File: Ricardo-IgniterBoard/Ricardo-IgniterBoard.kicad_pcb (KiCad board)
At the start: 4 copper layers, 76 parts, among them J1 RBUS, J2 USB_C_Receptacle_USB2.0, U1 ESP32-S3, U2 SN65HVD230, U3 LM66200DRLR, U4 MAX77827AEFD+T, U5 SC4215ASTRT, Y1 R940000171

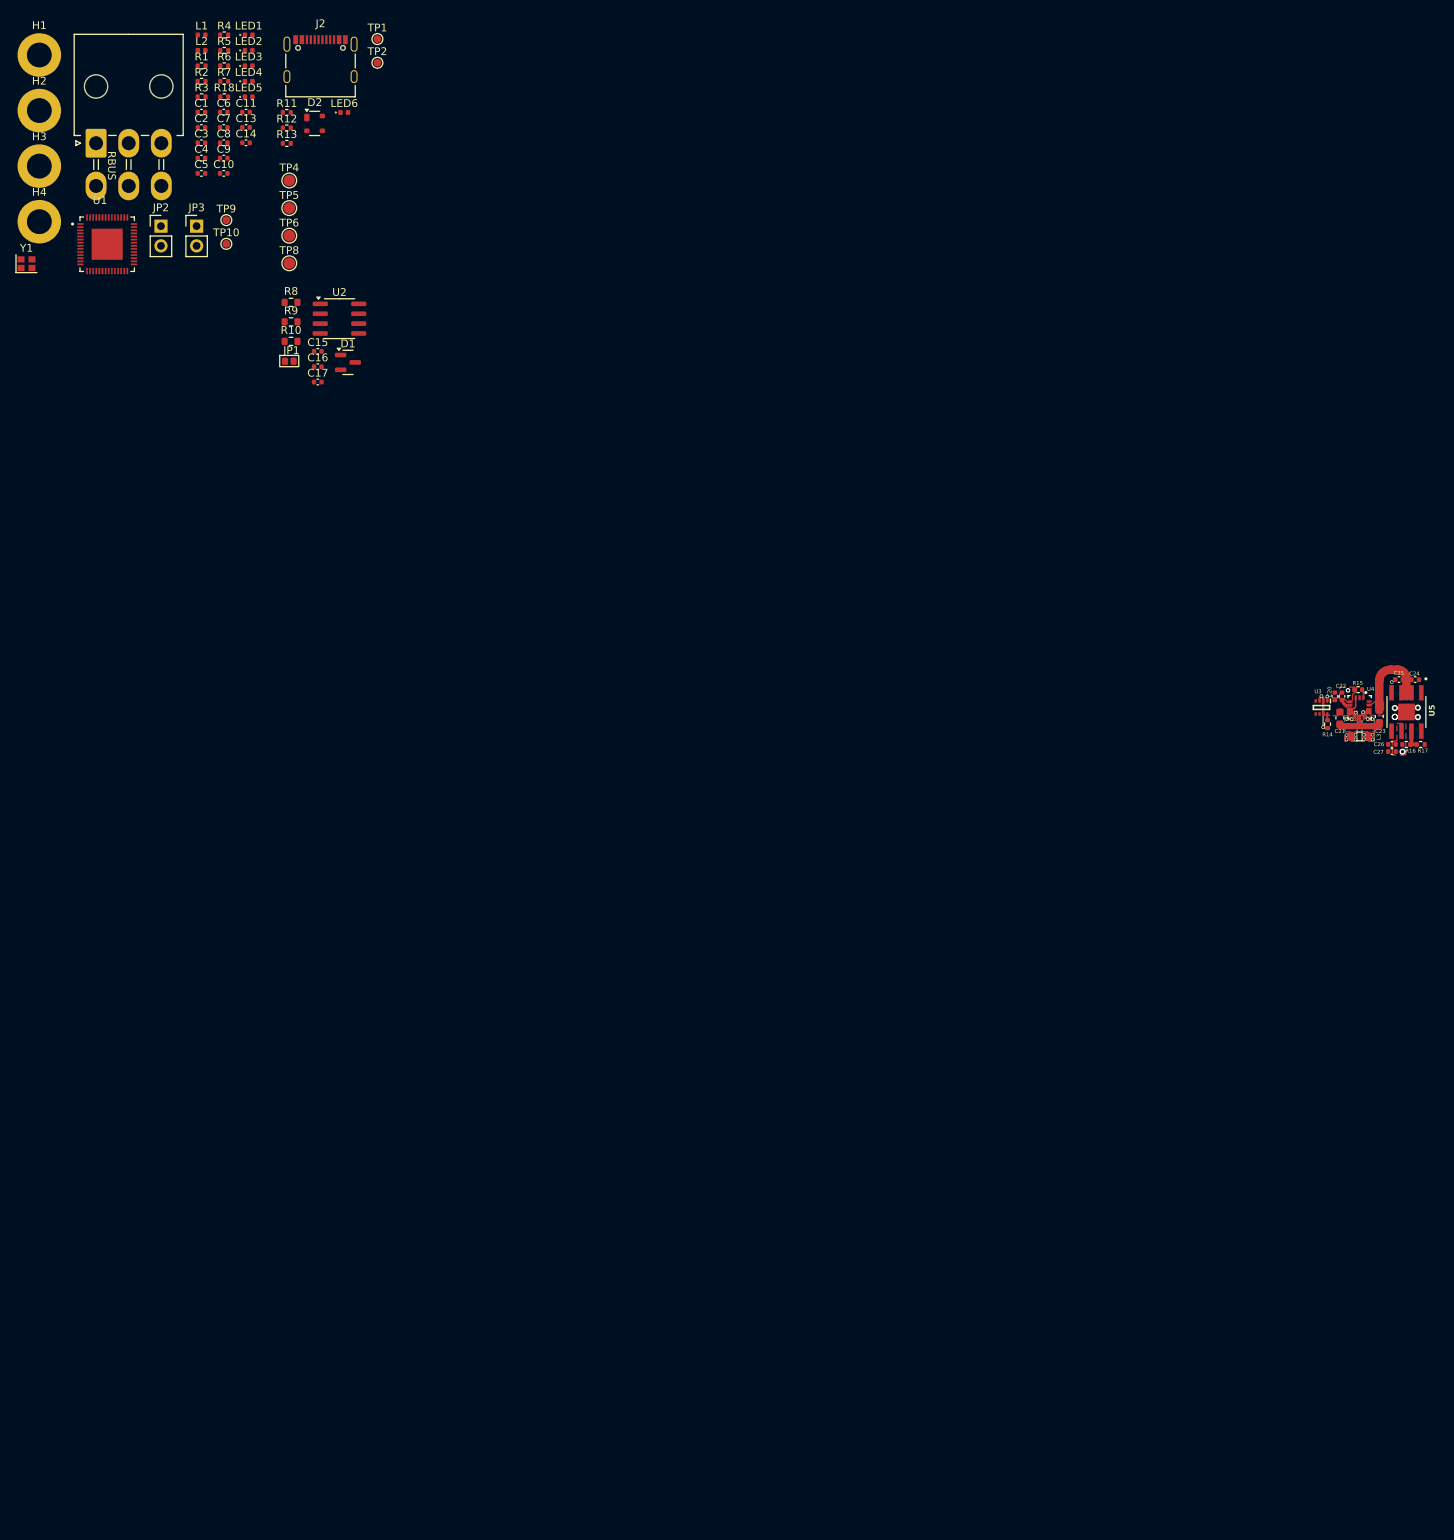
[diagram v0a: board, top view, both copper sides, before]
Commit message: Assigning components
And added the thermocouple
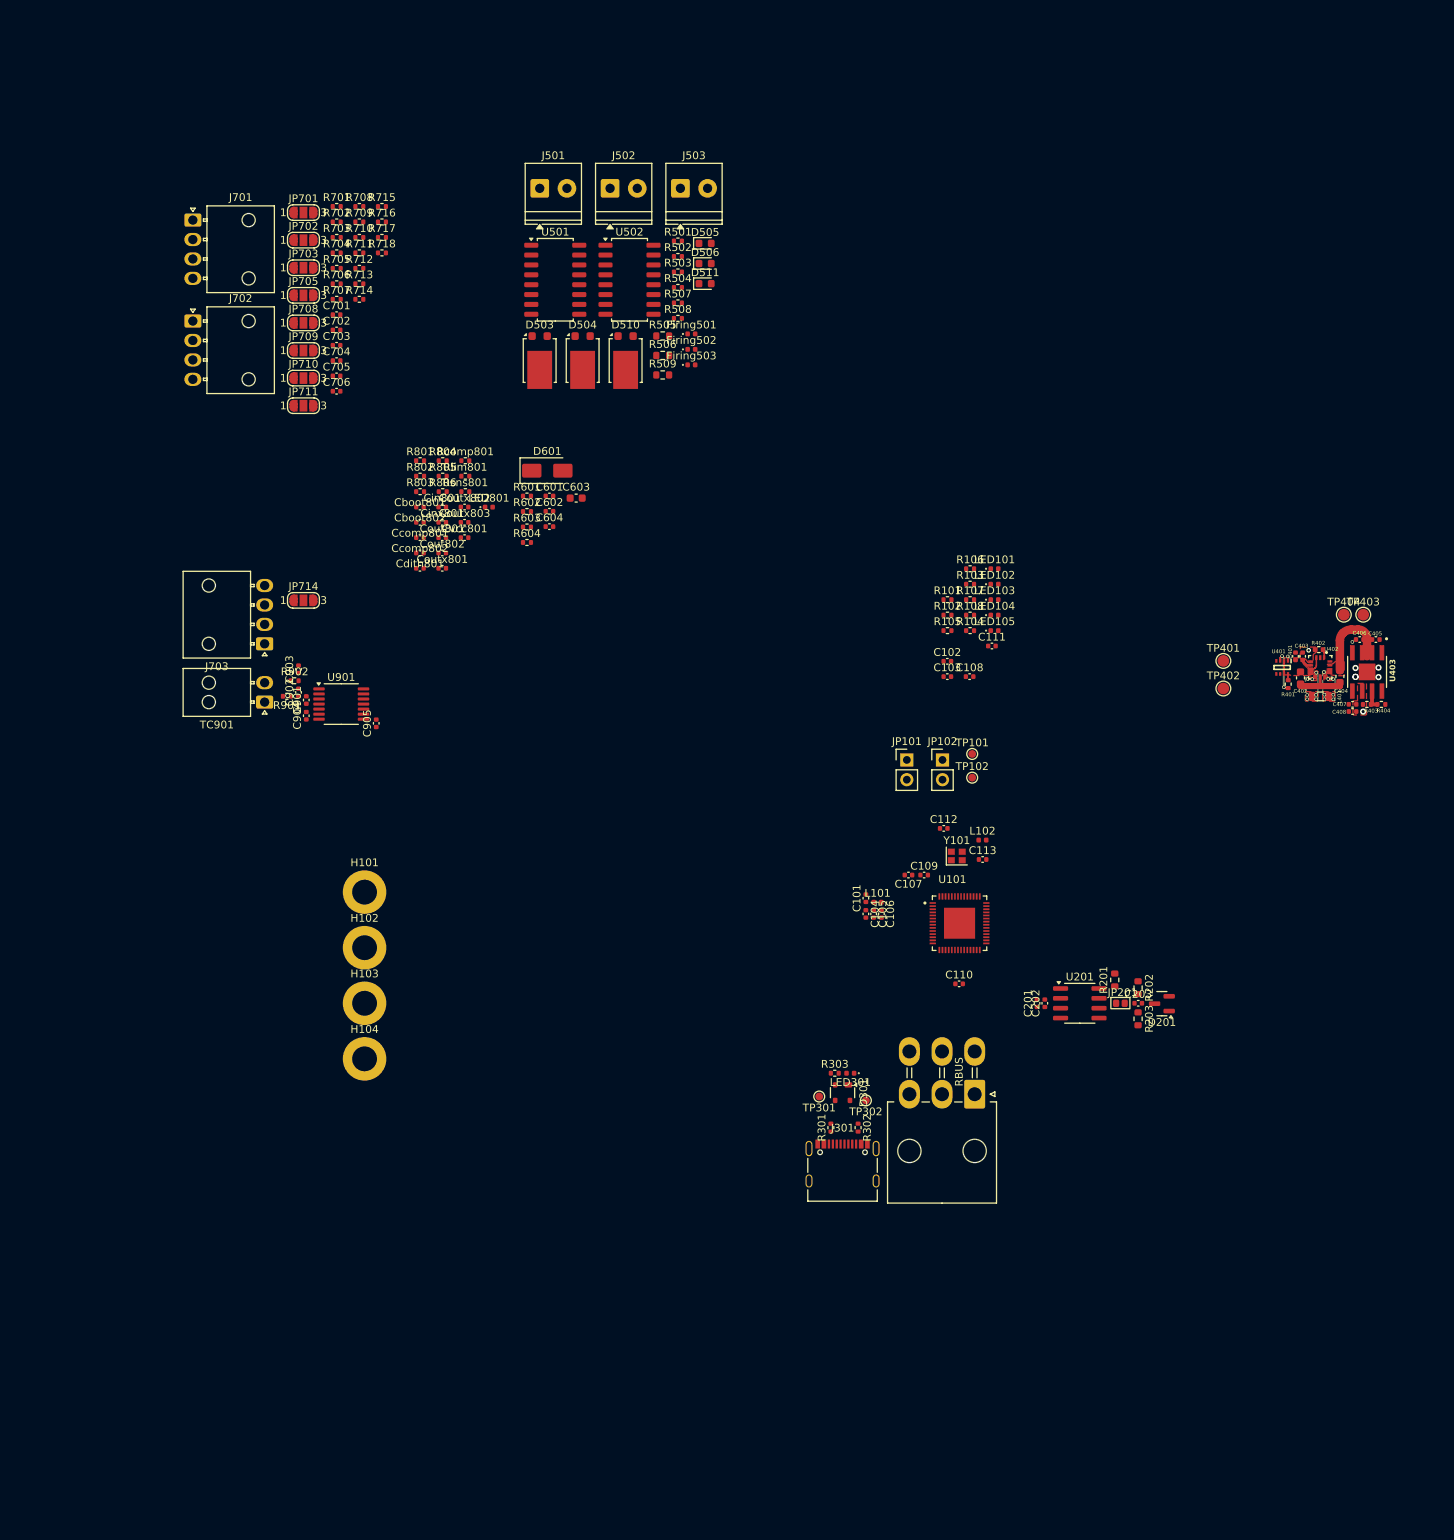
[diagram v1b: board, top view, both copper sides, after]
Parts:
- added C601: 0.1uF, Capacitor_SMD:C_0402_1005Metric, F.Cu at (68.7, 59.8)
- added C602: 1uF, Capacitor_SMD:C_0402_1005Metric, F.Cu at (68.7, 61.8)
- added C603: 0.1uF, Capacitor_SMD:C_0603_1608Metric, F.Cu at (72.2, 60.1)
- added C604: 0.1uF, Capacitor_SMD:C_0402_1005Metric, F.Cu at (68.7, 63.8)
- added C701: 1uF, Capacitor_SMD:C_0402_1005Metric, F.Cu at (41.3, 36.5)
- added C702: 1uF, Capacitor_SMD:C_0402_1005Metric, F.Cu at (41.3, 38.5)
- added C703: 220nF, Capacitor_SMD:C_0402_1005Metric, F.Cu at (41.3, 40.4)
- added C704: 10nF, Capacitor_SMD:C_0402_1005Metric, F.Cu at (41.3, 42.4)
- added C705: 10nF, Capacitor_SMD:C_0402_1005Metric, F.Cu at (41.3, 44.4)
- added C706: 10nF, Capacitor_SMD:C_0402_1005Metric, F.Cu at (41.3, 46.3)
- added C901: 0.01uF, Capacitor_SMD:C_0402_1005Metric, F.Cu at (37.4, 86.1)
- added C902: 0.1uF, Capacitor_SMD:C_0402_1005Metric, F.Cu at (36.4, 85.1)
- added C903: 0.01uF, Capacitor_SMD:C_0402_1005Metric, F.Cu at (36.4, 82.1)
- added C904: 0.1uF, Capacitor_SMD:C_0402_1005Metric, F.Cu at (37.4, 88.1)
- added C905: 0.1uF, Capacitor_SMD:C_0402_1005Metric, F.Cu at (46.4, 89.1)
- added Cboot801: 100nF, Capacitor_SMD:C_0402_1005Metric, F.Cu at (52.0, 61.2)
- added Cboot802: 100nF, Capacitor_SMD:C_0402_1005Metric, F.Cu at (52.0, 63.2)
- added Ccomp801: 15pF, Capacitor_SMD:C_0402_1005Metric, F.Cu at (52.0, 65.2)
- added Ccomp802: 2.2nF, Capacitor_SMD:C_0402_1005Metric, F.Cu at (52.0, 67.2)
- added Cdith801: 8.2nF, Capacitor_SMD:C_0402_1005Metric, F.Cu at (52.0, 69.1)
- added Cin801: 82uF, Capacitor_SMD:C_0402_1005Metric, F.Cu at (54.9, 61.2)
- added Cinx801: 10uF, Capacitor_SMD:C_0402_1005Metric, F.Cu at (54.9, 63.2)
- added Cout801: 56uF, Capacitor_SMD:C_0402_1005Metric, F.Cu at (54.9, 65.2)
- added Cout802: 56uF, Capacitor_SMD:C_0402_1005Metric, F.Cu at (54.9, 67.2)
- added Coutx801: 15uF, Capacitor_SMD:C_0402_1005Metric, F.Cu at (54.9, 69.1)
- added Coutx802: 15uF, Capacitor_SMD:C_0402_1005Metric, F.Cu at (57.8, 61.2)
- added Coutx803: 15uF, Capacitor_SMD:C_0402_1005Metric, F.Cu at (57.8, 63.2)
- added Cvcc801: 4.7uF, Capacitor_SMD:C_0402_1005Metric, F.Cu at (57.8, 65.2)
- added D503: DST1550S, Package_TO_SOT_SMD:TO-277B, F.Cu at (67.5, 42.4)
- added D504: DST1550S, Package_TO_SOT_SMD:TO-277B, F.Cu at (73.0, 42.4)
- added D505: RED_LED, LED_SMD:LED_0603_1608Metric, F.Cu at (88.7, 27.3)
- added D506: RED_LED, LED_SMD:LED_0603_1608Metric, F.Cu at (88.7, 29.9)
- added D510: DST1550S, Package_TO_SOT_SMD:TO-277B, F.Cu at (78.5, 42.4)
- added D511: RED_LED, LED_SMD:LED_0603_1608Metric, F.Cu at (88.7, 32.5)
- added D601: P6SMBJ28CA, Diode_SMD:D_SMA, F.Cu at (68.4, 56.6)
- added Firing501: EMERALD_LED, LED_SMD:LED_0402_1005Metric, F.Cu at (87.0, 39.0)
- added Firing502: EMERALD_LED, LED_SMD:LED_0402_1005Metric, F.Cu at (87.0, 41.0)
- added Firing503: EMERALD_LED, LED_SMD:LED_0402_1005Metric, F.Cu at (87.0, 42.9)
- added J501: Conn_01x02_Male, TerminalBlock_Phoenix:TerminalBlock_Phoenix_PT-1,5-2-3.5-H_1x02_P3.50mm_Horizontal, F.Cu at (67.5, 20.2)
- added J502: Conn_01x02_Male, TerminalBlock_Phoenix:TerminalBlock_Phoenix_PT-1,5-2-3.5-H_1x02_P3.50mm_Horizontal, F.Cu at (76.5, 20.2)
- added J503: Conn_01x02_Male, TerminalBlock_Phoenix:TerminalBlock_Phoenix_PT-1,5-2-3.5-H_1x02_P3.50mm_Horizontal, F.Cu at (85.6, 20.2)
- added J701: 1053131104, Connector_Molex:Molex_Nano-Fit_105313-xx04_1x04_P2.50mm_Horizontal, F.Cu at (22.8, 24.3)
- added J702: 1053131104, Connector_Molex:Molex_Nano-Fit_105313-xx04_1x04_P2.50mm_Horizontal, F.Cu at (22.8, 37.3)
- added J703: 1053131104, Connector_Molex:Molex_Nano-Fit_105313-xx04_1x04_P2.50mm_Horizontal, F.Cu at (32.1, 78.8)
- added JP701: SolderJumper_3_Open, Jumper:SolderJumper-3_P1.3mm_Open_RoundedPad1.0x1.5mm_NumberLabels, F.Cu at (37.1, 23.4)
- added JP702: SolderJumper_3_Open, Jumper:SolderJumper-3_P1.3mm_Open_RoundedPad1.0x1.5mm_NumberLabels, F.Cu at (37.1, 26.9)
- added JP703: SolderJumper_3_Open, Jumper:SolderJumper-3_P1.3mm_Open_RoundedPad1.0x1.5mm_NumberLabels, F.Cu at (37.1, 30.4)
- added JP705: SolderJumper_3_Open, Jumper:SolderJumper-3_P1.3mm_Open_RoundedPad1.0x1.5mm_NumberLabels, F.Cu at (37.1, 34.0)
- added JP708: SolderJumper_3_Open, Jumper:SolderJumper-3_P1.3mm_Open_RoundedPad1.0x1.5mm_NumberLabels, F.Cu at (37.1, 37.5)
- added JP709: SolderJumper_3_Open, Jumper:SolderJumper-3_P1.3mm_Open_RoundedPad1.0x1.5mm_NumberLabels, F.Cu at (37.1, 41.1)
- added JP710: SolderJumper_3_Open, Jumper:SolderJumper-3_P1.3mm_Open_RoundedPad1.0x1.5mm_NumberLabels, F.Cu at (37.1, 44.6)
- added JP711: SolderJumper_3_Open, Jumper:SolderJumper-3_P1.3mm_Open_RoundedPad1.0x1.5mm_NumberLabels, F.Cu at (37.1, 48.2)
- added JP714: SolderJumper_3_Open, Jumper:SolderJumper-3_P1.3mm_Open_RoundedPad1.0x1.5mm_NumberLabels, F.Cu at (37.1, 73.2)
- added LED801: RED_LED, LED_SMD:LED_0402_1005Metric, F.Cu at (60.9, 61.2)
- added R501: 120, Resistor_SMD:R_0402_1005Metric, F.Cu at (85.2, 27.0)
- added R502: 120, Resistor_SMD:R_0402_1005Metric, F.Cu at (85.2, 29.0)
- added R503: 10K, Resistor_SMD:R_0402_1005Metric, F.Cu at (85.2, 31.0)
- added R504: 10K, Resistor_SMD:R_0402_1005Metric, F.Cu at (85.2, 33.0)
- added R505: 120, Resistor_SMD:R_0603_1608Metric, F.Cu at (83.3, 39.2)
- added R506: 120, Resistor_SMD:R_0603_1608Metric, F.Cu at (83.3, 41.7)
- added R507: 120, Resistor_SMD:R_0402_1005Metric, F.Cu at (85.2, 35.0)
- added R508: 10K, Resistor_SMD:R_0402_1005Metric, F.Cu at (85.2, 37.0)
- added R509: 120, Resistor_SMD:R_0603_1608Metric, F.Cu at (83.3, 44.2)
- added R601: 10k, Resistor_SMD:R_0402_1005Metric, F.Cu at (65.8, 59.8)
- added R602: 100k, Resistor_SMD:R_0402_1005Metric, F.Cu at (65.8, 61.8)
- added R603: 5.1k, Resistor_SMD:R_0402_1005Metric, F.Cu at (65.8, 63.8)
- added R604: 4.22k, Resistor_SMD:R_0402_1005Metric, F.Cu at (65.8, 65.8)
- added R701: 75k, Resistor_SMD:R_0402_1005Metric, F.Cu at (41.3, 22.6)
- added R702: 14k, Resistor_SMD:R_0402_1005Metric, F.Cu at (41.3, 24.6)
- added R703: 10k, Resistor_SMD:R_0402_1005Metric, F.Cu at (41.3, 26.6)
- added R704: 75k, Resistor_SMD:R_0402_1005Metric, F.Cu at (41.3, 28.5)
- added R705: 14k, Resistor_SMD:R_0402_1005Metric, F.Cu at (41.3, 30.5)
- added R706: 10k, Resistor_SMD:R_0402_1005Metric, F.Cu at (41.3, 32.5)
- added R707: 1k, Resistor_SMD:R_0402_1005Metric, F.Cu at (41.3, 34.5)
- added R708: 1k, Resistor_SMD:R_0402_1005Metric, F.Cu at (44.2, 22.6)
- added R709: 49.9, Resistor_SMD:R_0402_1005Metric, F.Cu at (44.2, 24.6)
- added R710: 1k, Resistor_SMD:R_0402_1005Metric, F.Cu at (44.2, 26.6)
- added R711: 49.9, Resistor_SMD:R_0402_1005Metric, F.Cu at (44.2, 28.5)
- added R712: 1k, Resistor_SMD:R_0402_1005Metric, F.Cu at (44.2, 30.5)
- added R713: 75k, Resistor_SMD:R_0402_1005Metric, F.Cu at (44.2, 32.5)
- added R714: 14k, Resistor_SMD:R_0402_1005Metric, F.Cu at (44.2, 34.5)
- added R715: 10k, Resistor_SMD:R_0402_1005Metric, F.Cu at (47.2, 22.6)
- added R716: 1k, Resistor_SMD:R_0402_1005Metric, F.Cu at (47.2, 24.6)
- added R717: 49.9, Resistor_SMD:R_0402_1005Metric, F.Cu at (47.2, 26.6)
- added R718: 1k, Resistor_SMD:R_0402_1005Metric, F.Cu at (47.2, 28.5)
- added R801: 715k, Resistor_SMD:R_0402_1005Metric, F.Cu at (52.1, 55.3)
- added R802: 100k, Resistor_SMD:R_0402_1005Metric, F.Cu at (52.1, 57.3)
- added R803: 49.9k, Resistor_SMD:R_0402_1005Metric, F.Cu at (52.1, 59.3)
- added R804: 1, Resistor_SMD:R_0402_1005Metric, F.Cu at (55.0, 55.3)
- added R805: 1, Resistor_SMD:R_0402_1005Metric, F.Cu at (55.0, 57.3)
- added R806: 3k, Resistor_SMD:R_0402_1005Metric, F.Cu at (55.0, 59.3)
- added R901: 100, Resistor_SMD:R_0402_1005Metric, F.Cu at (34.9, 85.6)
- added R902: 100, Resistor_SMD:R_0402_1005Metric, F.Cu at (35.9, 83.6)
- added Rcomp801: 95.3k, Resistor_SMD:R_0402_1005Metric, F.Cu at (57.9, 55.3)
- added Rlim801: 31.6k, Resistor_SMD:R_0402_1005Metric, F.Cu at (57.9, 57.3)
- added Rsns801: 8.333m, Resistor_SMD:R_0402_1005Metric, F.Cu at (57.9, 59.3)
- added TC901: Thermocouple, Connector_Molex:Molex_Nano-Fit_105313-xx02_1x02_P2.50mm_Horizontal, F.Cu at (32.1, 86.3)
- added U501: LTV-247, Package_SO:SOP-16_4.4x10.4mm_P1.27mm, F.Cu at (69.5, 32.0)
- added U502: LTV-247, Package_SO:SOP-16_4.4x10.4mm_P1.27mm, F.Cu at (79.0, 32.0)
- added U901: MAX31856, Package_SO:TSSOP-14_4.4x5mm_P0.65mm, F.Cu at (41.9, 86.6)
- moved J101 166.6 mm to (123.4, 136.8), turned to 180 degrees
- moved J301 157.2 mm to (106.4, 145.7)
- moved R301 148.2 mm to (104.9, 141.1), turned to 90 degrees
- moved R302 148.1 mm to (108.4, 141.1), turned to -90 degrees
- moved TP302 147.6 mm to (109.4, 137.6), turned to 180 degrees
- moved TP301 147.5 mm to (103.4, 137.1), turned to 180 degrees
- moved TP403 146.5 mm to (173.4, 75.1)
- moved TP404 143.0 mm to (170.9, 75.1)
- moved L102 142.9 mm to (124.4, 104.1)
- moved D301 142.0 mm to (106.4, 136.6), turned to -90 degrees
- moved Y101 141.9 mm to (121.1, 106.1)
- moved L101 141.5 mm to (110.9, 112.1)
- moved C110 140.8 mm to (121.4, 122.6)
- moved U101 140.2 mm to (121.5, 114.8)
- moved LED301 139.7 mm to (107.4, 134.1), turned to 180 degrees
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- renumbered C1 to C101, C2 to C102, C3 to C103, C4 to C104, C5 to C105, C6 to C106, C7 to C107, C8 to C108, C9 to C109, C10 to C110, C11 to C111, C13 to C112, C14 to C113, C15 to C201, C16 to C202, C17 to C203, C20 to C401, C21 to C402, C22 to C403, C23 to C404, C24 to C405, C25 to C406, C26 to C407, C27 to C408, D1 to D201, D2 to D301, H1 to H101, H2 to H102, H3 to H103, H4 to H104, J1 to J101, J2 to J301, JP2 to JP101, JP3 to JP102, JP1 to JP201, L1 to L101, L2 to L102, L3 to L401, LED1 to LED101, LED2 to LED102, LED3 to LED103, LED4 to LED104, LED5 to LED105, LED6 to LED301, R1 to R101, R2 to R102, R5 to R103, R18 to R104, R3 to R105, R4 to R106, R6 to R107, R7 to R108, R8 to R201, R9 to R202, R10 to R203, R11 to R301, R12 to R302, R13 to R303, R14 to R401, R15 to R402, R16 to R403, R17 to R404, TP9 to TP101, TP10 to TP102, TP1 to TP301, TP2 to TP302, TP4 to TP401, TP5 to TP402, TP6 to TP403, TP8 to TP404, U1 to U101, U2 to U201, U3 to U401, U4 to U402, U5 to U403, Y1 to Y101
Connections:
- R108 pad 1: +12V -> +16.8V
- U101 pad 10: unconnected-(U1-GPIO5/ADC1_CH4-Pad10) -> /ADS_MOSI
- U101 pad 11: unconnected-(U1-GPIO6/ADC1_CH5-Pad11) -> /ADS_MISO
- U101 pad 12: unconnected-(U1-GPIO7/ADC1_CH6-Pad12) -> /ADS_CLK
- U101 pad 13: unconnected-(U1-GPIO8/ADC1_CH7-Pad13) -> /ADS_SCLK
- U101 pad 14: unconnected-(U1-GPIO9/ADC1_CH8-Pad14) -> /ADS_PT_DRDY
- U101 pad 15: unconnected-(U1-GPIO10/ADC1_CH9-Pad15) -> /ADS_PT_CS0
- U101 pad 16: unconnected-(U1-GPIO11/ADC2_CH0-Pad16) -> /SDA
- U101 pad 17: unconnected-(U1-GPIO12/ADC2_CH1-Pad17) -> /SCL
- U101 pad 18: unconnected-(U1-GPIO13/ADC2_CH2-Pad18) -> /CurrentSense
- U101 pad 19: unconnected-(U1-GPIO14/ADC2_CH3-Pad19) -> /BuckBoostProt
- U101 pad 23: unconnected-(U1-GPIO17/ADC2_CH6/DAC_2-Pad23) -> /CAN_RX
- U101 pad 24: unconnected-(U1-GPIO18/ADC2_CH7/DAC_1-Pad24) -> /CAN_TX
- U101 pad 38: unconnected-(U1-GPIO33-Pad38) -> /Nuke0
- U101 pad 39: unconnected-(U1-GPIO34-Pad39) -> /Nuke1
- U101 pad 40: unconnected-(U1-GPIO35-Pad40) -> /Nuke2
- U101 pad 42: unconnected-(U1-GPIO37-Pad42) -> /Cont0
- U101 pad 43: unconnected-(U1-GPIO38-Pad43) -> /Cont1
- U101 pad 44: unconnected-(U1-MTCK/JTAG/GPIO39-Pad44) -> /BUS_VMON
- U101 pad 45: unconnected-(U1-MTDO/JTAG/GPIO40-Pad45) -> /HSIDE_EN
- U101 pad 51: unconnected-(U1-GPIO45-Pad51) -> /Cont2
- U101 pad 6: unconnected-(U1-GPIO1/ADC1_CH0-Pad6) -> /ADS_TC_CS
- U101 pad 7: unconnected-(U1-GPIO2/ADC1_CH1-Pad7) -> /ADS_TC_FAULT
- U101 pad 9: unconnected-(U1-GPIO4/ADC1_CH3-Pad9) -> /ADS_TC_DRDY

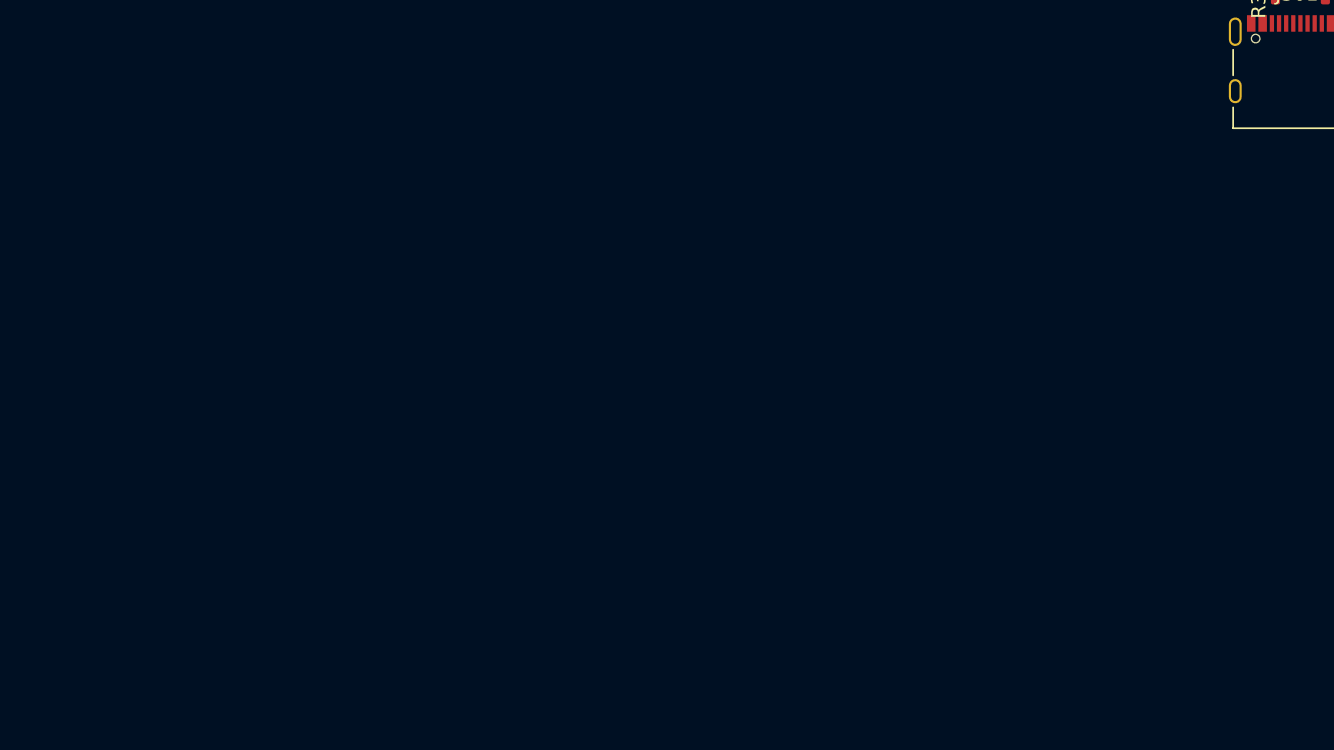
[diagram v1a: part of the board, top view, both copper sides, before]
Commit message: Assigning footprints
and adding them to layout
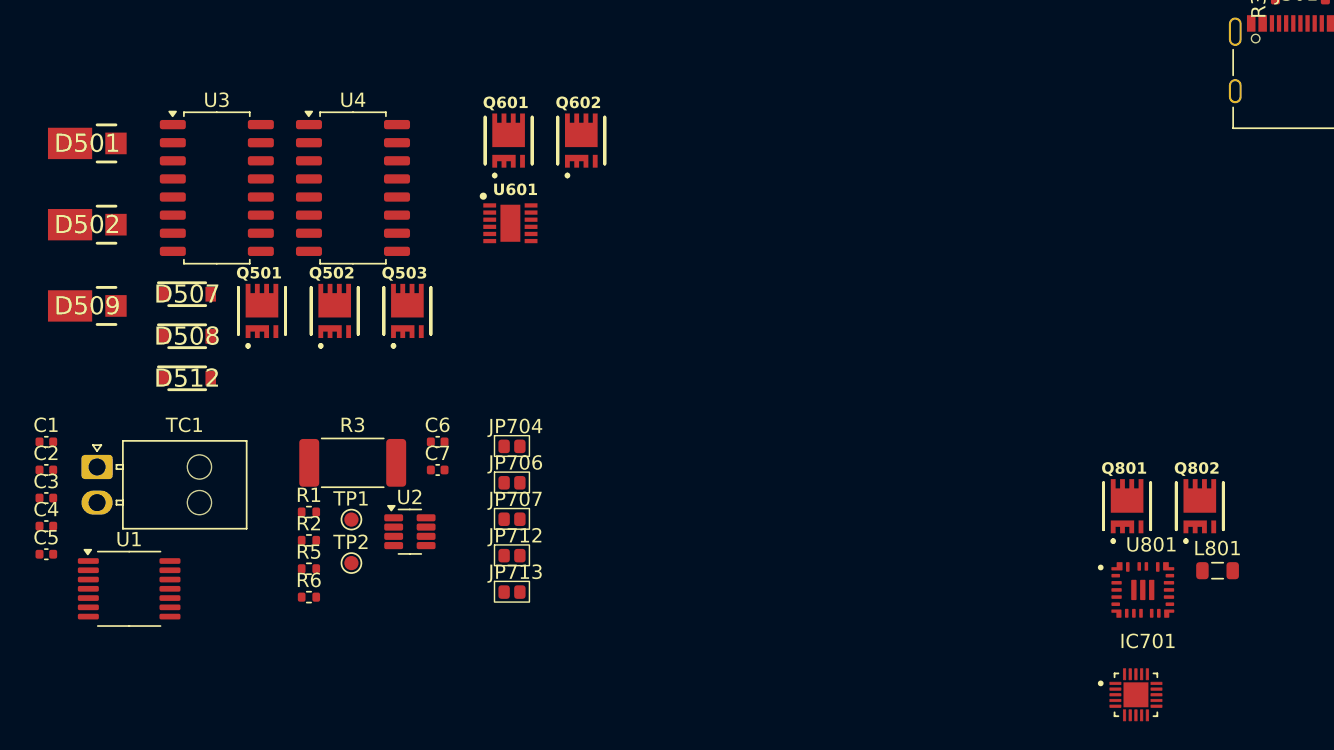
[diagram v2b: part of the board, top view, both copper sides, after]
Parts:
- added C1: 100nF, Capacitor_SMD:C_0402_1005Metric, F.Cu at (18.7, 172.6)
- added C2: 100nF, Capacitor_SMD:C_0402_1005Metric, F.Cu at (18.7, 174.5)
- added C3: 10nF, Capacitor_SMD:C_0402_1005Metric, F.Cu at (18.7, 176.5)
- added C4: 100nF, Capacitor_SMD:C_0402_1005Metric, F.Cu at (18.7, 178.5)
- added C5: 10nF, Capacitor_SMD:C_0402_1005Metric, F.Cu at (18.7, 180.4)
- added C6: 0.1uF, Capacitor_SMD:C_0402_1005Metric, F.Cu at (46.2, 172.6)
- added C7: 0.1uF, Capacitor_SMD:C_0402_1005Metric, F.Cu at (46.2, 174.5)
- added D501: V8PAM10S-M3/I, iclr:V8PAM10SM3I, F.Cu at (21.5, 151.6)
- added D502: V8PAM10S-M3/I, iclr:V8PAM10SM3I, F.Cu at (21.5, 157.3)
- added D507: S-102T, iclr:SODFL3516X70N, F.Cu at (28.6, 162.2)
- added D508: S-102T, iclr:SODFL3516X70N, F.Cu at (28.6, 165.1)
- added D509: V8PAM10S-M3/I, iclr:V8PAM10SM3I, F.Cu at (21.5, 163.0)
- added D512: S-102T, iclr:SODFL3516X70N, F.Cu at (28.6, 168.1)
- added IC701: ADS131M04IRUKR, iclr:ADS131M04IRUKR, F.Cu at (95.1, 190.3)
- added JP704: SolderJumper_2_Open, iclr:SmallerSolderJP, F.Cu at (51.6, 172.9)
- added JP706: SolderJumper_2_Open, iclr:SmallerSolderJP, F.Cu at (51.6, 175.4)
- added JP707: SolderJumper_2_Open, iclr:SmallerSolderJP, F.Cu at (51.6, 178.0)
- added JP712: SolderJumper_2_Open, iclr:SmallerSolderJP, F.Cu at (51.6, 180.5)
- added JP713: SolderJumper_2_Open, iclr:SmallerSolderJP, F.Cu at (51.6, 183.1)
- added L801: 5.6uH, Inductor_SMD:L_0805_2012Metric, F.Cu at (100.9, 181.6)
- added Q501: BSZ025N04LS, iclr:BSZ025N04LS, F.Cu at (33.8, 163.4)
- added Q502: BSZ025N04LS, iclr:BSZ025N04LS, F.Cu at (38.9, 163.4)
- added Q503: BSZ025N04LS, iclr:BSZ025N04LS, F.Cu at (44.0, 163.4)
- added Q601: BSZ025N04LS, iclr:BSZ025N04LS, F.Cu at (51.1, 151.4)
- added Q602: BSZ025N04LS, iclr:BSZ025N04LS, F.Cu at (56.2, 151.4)
- added Q801: NMOS, iclr:BSZ025N04LS, F.Cu at (94.5, 177.1)
- added Q802: NMOS, iclr:BSZ025N04LS, F.Cu at (99.6, 177.1)
- added R1: 10, Resistor_SMD:R_0402_1005Metric, F.Cu at (37.1, 177.5)
- added R2: 10, Resistor_SMD:R_0402_1005Metric, F.Cu at (37.1, 179.5)
- added R3: 2m, Resistor_SMD:R_2512_6332Metric_Pad1.40x3.35mm_HandSolder, F.Cu at (40.2, 174.0)
- added R5: 10k, Resistor_SMD:R_0402_1005Metric, F.Cu at (37.1, 181.5)
- added R6: 10k, Resistor_SMD:R_0402_1005Metric, F.Cu at (37.1, 183.4)
- added TC1: Thermocouple, Connector_Molex:Molex_Nano-Fit_105313-xx02_1x02_P2.50mm_Horizontal, F.Cu at (22.3, 174.3)
- added TP1: TestPoint, TestPoint:TestPoint_Pad_D1.0mm, F.Cu at (40.1, 178.0)
- added TP2: TestPoint, TestPoint:TestPoint_Pad_D1.0mm, F.Cu at (40.1, 181.1)
- added U1: MAX31856, Package_SO:TSSOP-14_4.4x5mm_P0.65mm, F.Cu at (24.5, 182.9)
- added U2: INA219AxDCN, Package_TO_SOT_SMD:SOT-23-8, F.Cu at (44.2, 178.9)
- added U3: LTV-247, Package_SO:SOP-16_4.4x10.4mm_P1.27mm, F.Cu at (30.7, 154.7)
- added U4: LTV-247, Package_SO:SOP-16_4.4x10.4mm_P1.27mm, F.Cu at (40.2, 154.7)
- added U601: LM74810, iclr:SON50P300X300X80-13N-D, F.Cu at (51.3, 157.2)
- added U801: TPS55288QRPMRQ1, iclr:CONV_TPS552882QRPMRQ1, F.Cu at (95.6, 182.9)
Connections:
- J501 pad 1: /PyroPwr -> /DeployPWR
- J502 pad 1: /PyroPwr -> /DeployPWR
- J503 pad 1: /PyroPwr -> /IgniterPWR
- R806 pad 1: /PyroPwr -> /IgniterPWR
- Rsns801 pad 2: /PyroPwr -> /IgniterPWR
- U101 pad 6: /ADS_TC_CS -> /tcCS
- U101 pad 7: /ADS_TC_FAULT -> /tcFAULT
- U101 pad 9: /ADS_TC_DRDY -> /tcDRDY
